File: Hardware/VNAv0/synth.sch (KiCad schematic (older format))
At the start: 35 parts, among them U3 MAX2871, X1 ASTXR-12-19.200MHz

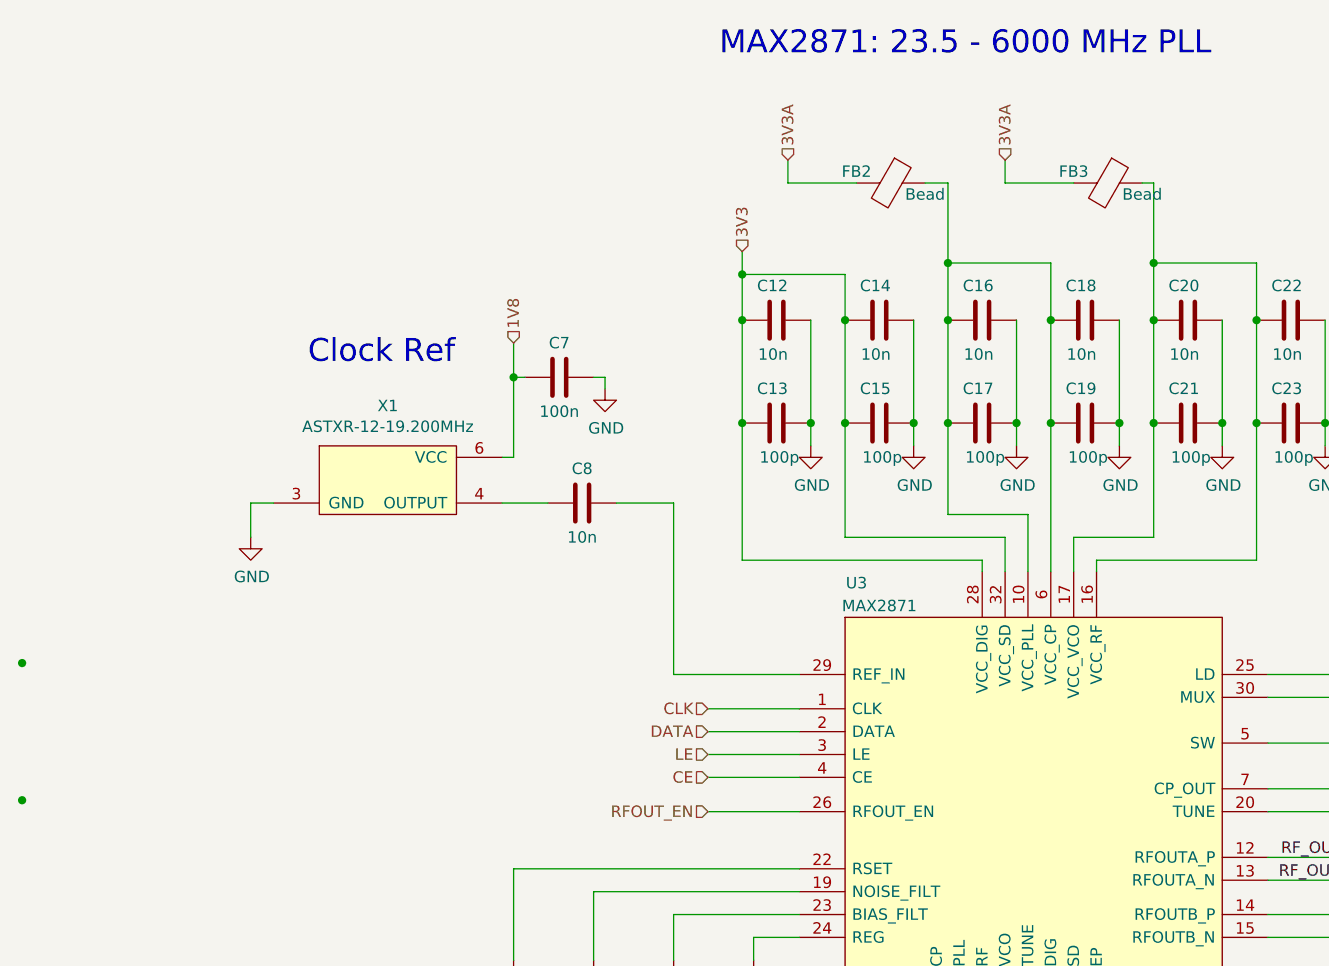
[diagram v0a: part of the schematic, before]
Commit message: tx chain now works, however output power too low
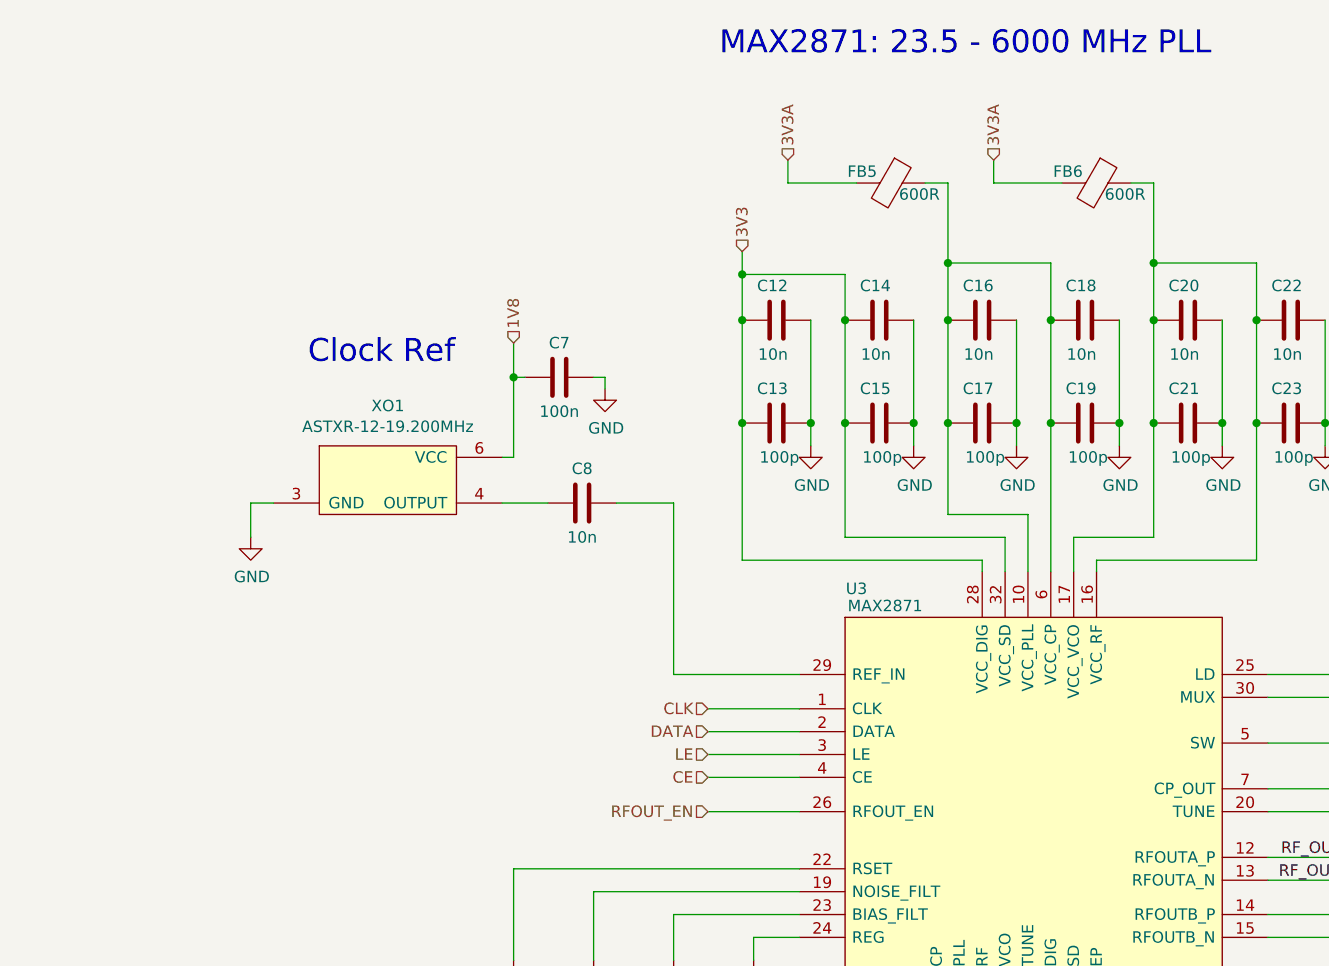
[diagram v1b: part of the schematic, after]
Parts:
- removed FB2, FB3: Bead, VNA_Footprints:BEADC1608X95N, symbol VNA_Symbols:Ferrite_Bead_PWR
- removed X1: ASTXR-12-19.200MHz, VNA_Footprints:ASTXR-12, symbol VNA_Symbols:ASTXR-12-19.200MHz
- added FB5, FB6: 600R, symbol VNA_Symbols:Ferrite_Bead_PWR
- added XO1: ASTXR-12-19.200MHz, symbol VNA_Symbols:ASTXR-12-19.200MHz
- U3: footprint VNA_Footprints:QFN-32-1EP_5x5mm_Pitch0.5mm_Thermal_Vias -> (none)
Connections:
- net 1V8: now also XO1.6 (VCC)
- net 3V3A: now also FB5.2, FB6.2
- net GND: now also XO1.3 (GND)
- net at C8.2: now also XO1.4 (OUTPUT)
- net at C16.1, C17.1, C18.1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: now also FB5.1
- net at C20.1, C21.1, C22.1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: now also FB6.1
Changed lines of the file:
@@
 	4050 2250 4500 2250
 Wire Wire Line
-	4900 1900 4950 1900
+	4850 1900 4950 1900
 Wire Wire Line
 	4950 2250 5400 2250
@@
 	1    0    0    -1
 $EndComp
-Connection ~ 0    4000
 Wire Wire Line
 	10000 4000 10000 4100
@@
 	3350 1900 3650 1900
 Wire Wire Line
-	4300 1900 4300 1800
-Wire Wire Line
-	4300 1900 4600 1900
+	4250 1900 4250 1800
+Wire Wire Line
+	4250 1900 4550 1900
 Wire Wire Line
 	5900 5250 5900 5200
@@
 Wire Wire Line
 	9600 4600 10000 4600
-$Comp
-L VNA_Symbols:ASTXR-12-19.200MHz X1
-U 1 1 5C321785
-P 1500 3150
-F 0 "X1" H 1600 3425 50  0000 C CNN
-F 1 "ASTXR-12-19.200MHz" H 1600 3334 50  0000 C CNN
-F 2 "VNA_Footprints:ASTXR-12" H 1400 3300 50  0001 C CNN
-F 3 "" H 1400 3300 50  0001 C CNN
-	1    1500 3150
-	1    0    0    -1
-$EndComp
 Wire Wire Line
 	2100 3300 2300 3300
-$Comp
-L VNA_Symbols:MAX2871 U3
-U 1 1 5C32C1BE
-P 4400 4650
-F 0 "U3" H 3650 5650 50  0000 C CNN
-F 1 "MAX2871" H 3750 5550 50  0000 C CNN
-F 2 "VNA_Footprints:QFN-32-1EP_5x5mm_Pitch0.5mm_Thermal_Vias" H 5600 5800 50  0001 L CNN
-F 3 "https://componentsearchengine.com/Datasheets/1/MAX2871ETJ+.pdf" H 4850 5550 50  0001 L CNN
-	1    4400 4650
-	1    0    0    -1
-$EndComp
 Wire Wire Line
 	9600 5100 10300 5100
 Wire Wire Line
 	10000 4400 10000 4600
-Connection ~ 0    4600
 Wire Wire Line
 	10000 4600 10300 4600
@@
 Text HLabel 3350 1800 1    50   Input ~ 0
 3V3A
-Text HLabel 4300 1800 1    50   Input ~ 0
+Text HLabel 4250 1800 1    50   Input ~ 0
 3V3A
 Text HLabel 6400 5000 1    50   Input ~ 0
@@
 Text HLabel 3150 2200 1    50   Input ~ 0
 3V3
-$Comp
-L VNA_Symbols:Ferrite_Bead_PWR FB?
-U 1 1 5CCC81FC
-P 3800 1900
-AR Path="/5CCC81FC" Ref="FB?"  Part="1"
-AR Path="/5CA81007/5CCC81FC" Ref="FB2"  Part="1"
-F 0 "FB2" V 3750 1750 50  0000 C CNN
-F 1 "Bead" V 3850 2050 50  0000 C CNN
-F 2 "VNA_Footprints:BEADC1608X95N" V 3730 1900 50  0001 C CNN
-F 3 "~" H 3800 1900 50  0001 C CNN
-	1    3800 1900
-	0    1    1    0
-$EndComp
-$Comp
-L VNA_Symbols:Ferrite_Bead_PWR FB?
-U 1 1 5CCCD1B3
-P 4750 1900
-AR Path="/5CCCD1B3" Ref="FB?"  Part="1"
-AR Path="/5CA81007/5CCCD1B3" Ref="FB3"  Part="1"
-F 0 "FB3" V 4700 1750 50  0000 C CNN
-F 1 "Bead" V 4800 2050 50  0000 C CNN
-F 2 "VNA_Footprints:BEADC1608X95N" V 4680 1900 50  0001 C CNN
-F 3 "~" H 4750 1900 50  0001 C CNN
-	1    4750 1900
-	0    1    1    0
-$EndComp
 Wire Wire Line
 	7300 4300 7850 4300
@@
 Wire Wire Line
 	8850 4300 9000 4300
+$Comp
+L VNA_Symbols:ASTXR-12-19.200MHz XO1
+U 1 1 5D15B7DE
+P 1500 3150
+F 0 "XO1" H 1600 3425 50  0000 C CNN
+F 1 "ASTXR-12-19.200MHz" H 1600 3334 50  0000 C CNN
+F 2 "" H 1400 3300 50  0001 C CNN
+F 3 "" H 1400 3300 50  0001 C CNN
+	1    1500 3150
+	1    0    0    -1
+$EndComp
+$Comp
+L VNA_Symbols:MAX2871 U3
+U 1 1 5D15C200
+P 4400 4650
+F 0 "U3" H 3650 5625 50  0000 C CNN
+F 1 "MAX2871" H 3775 5550 50  0000 C CNN
+F 2 "" H 5600 5800 50  0001 L CNN
+F 3 "" H 4850 5550 50  0001 L CNN
+	1    4400 4650
+	1    0    0    -1
+$EndComp
+$Comp
+L VNA_Symbols:Ferrite_Bead_PWR FB5
+U 1 1 5D19C9EF
+P 3800 1900
+F 0 "FB5" V 3750 1775 50  0000 C CNN
+F 1 "600R" V 3850 2025 50  0000 C CNN
+F 2 "" V 3730 1900 50  0001 C CNN
+F 3 "~" H 3800 1900 50  0001 C CNN
+	1    3800 1900
+	0    1    1    0
+$EndComp
+$Comp
+L VNA_Symbols:Ferrite_Bead_PWR FB6
+U 1 1 5D19D7ED
+P 4700 1900
+F 0 "FB6" V 4650 1775 50  0000 C CNN
+F 1 "600R" V 4750 2025 50  0000 C CNN
+F 2 "" V 4630 1900 50  0001 C CNN
+F 3 "~" H 4700 1900 50  0001 C CNN
+	1    4700 1900
+	0    1    1    0
+$EndComp
 $EndSCHEMATC
